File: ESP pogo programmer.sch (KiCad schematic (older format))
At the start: 3 parts

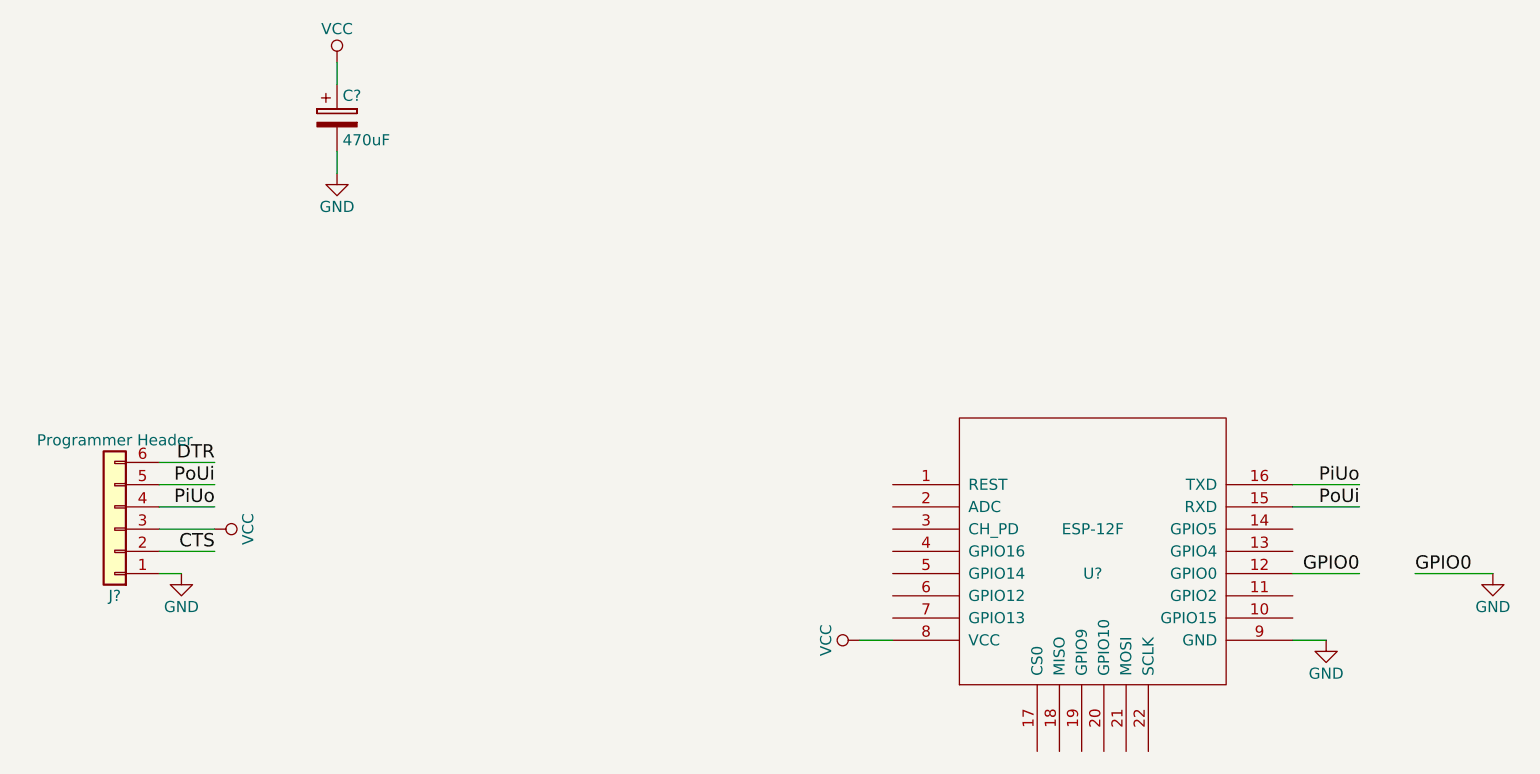
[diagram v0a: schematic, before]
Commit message: Schematic and footprints done
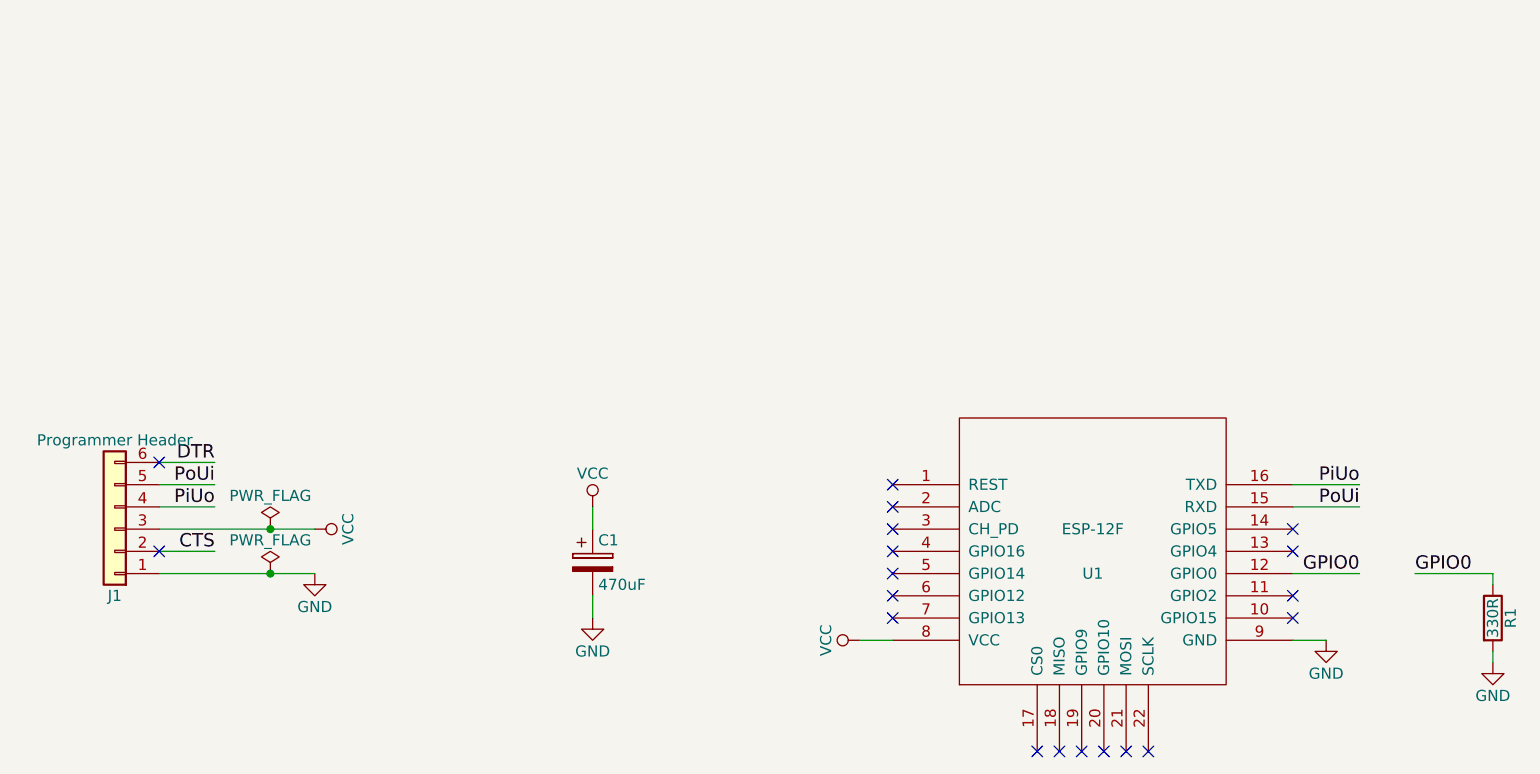
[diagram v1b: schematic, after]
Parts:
- added R1: 330R, Resistors_THT:R_Axial_DIN0207_L6.3mm_D2.5mm_P7.62mm_Horizontal, symbol R
- C1: renamed from C?; footprint (none) -> Capacitors_THT:CP_Radial_D6.3mm_P2.50mm
- J1: renamed from J?; footprint (none) -> Socket_Strips:Socket_Strip_Straight_1x06_Pitch2.54mm
- U1: renamed from U?; footprint (none) -> ESP-pogo-programmer_local:ESP-12F-pgrm
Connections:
- net GND: now also R1.2; no longer U1.12 (GPIO0)
- new net GPIO0: R1.1, U1.12 (GPIO0)
- no-connect marks 0 -> 19
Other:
- moved on the sheet: C1
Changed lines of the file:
@@
 $EndDescr
 $Comp
-L Conn_01x06 J?
+L Conn_01x06 J1
 U 1 1 5AC77FF5
 P 1550 3900
-F 0 "J?" H 1550 4200 50  0000 C CNN
+F 0 "J1" H 1550 4200 50  0000 C CNN
 F 1 "Programmer Header" H 1550 3500 50  0000 C CNN
-F 2 "" H 1550 3900 50  0001 C CNN
+F 2 "Socket_Strips:Socket_Strip_Straight_1x06_Pitch2.54mm" H 1550 3900 50  0001 C CNN
 F 3 "" H 1550 3900 50  0001 C CNN
 	1    1550 3900
@@
 $EndComp
 $Comp
-L GND #PWR?
+L GND #PWR01
 U 1 1 5AC78376
-P 1850 4100
-F 0 "#PWR?" H 1850 3850 50  0001 C CNN
-F 1 "GND" H 1850 3950 50  0000 C CNN
-F 2 "" H 1850 4100 50  0001 C CNN
-F 3 "" H 1850 4100 50  0001 C CNN
-	1    1850 4100
-	1    0    0    -1
-$EndComp
-Wire Wire Line
-	1750 4100 1850 4100
-$Comp
-L VCC #PWR?
+P 2450 4100
+F 0 "#PWR01" H 2450 3850 50  0001 C CNN
+F 1 "GND" H 2450 3950 50  0000 C CNN
+F 2 "" H 2450 4100 50  0001 C CNN
+F 3 "" H 2450 4100 50  0001 C CNN
+	1    2450 4100
+	1    0    0    -1
+$EndComp
+$Comp
+L VCC #PWR02
 U 1 1 5AC7838F
-P 2000 3900
-F 0 "#PWR?" H 2000 3750 50  0001 C CNN
-F 1 "VCC" H 2000 4050 50  0000 C CNN
-F 2 "" H 2000 3900 50  0001 C CNN
-F 3 "" H 2000 3900 50  0001 C CNN
-	1    2000 3900
+P 2450 3900
+F 0 "#PWR02" H 2450 3750 50  0001 C CNN
+F 1 "VCC" H 2450 4050 50  0000 C CNN
+F 2 "" H 2450 3900 50  0001 C CNN
+F 3 "" H 2450 3900 50  0001 C CNN
+	1    2450 3900
 	0    1    1    0
 $EndComp
-Wire Wire Line
-	1750 3900 2000 3900
 Text Label 2000 3800 2    60   ~ 0
 PiUo
@@
 	2000 3700 1750 3700
 $Comp
-L VCC #PWR?
+L VCC #PWR03
 U 1 1 5AC783EB
-P 2550 1800
-F 0 "#PWR?" H 2550 1650 50  0001 C CNN
-F 1 "VCC" H 2550 1950 50  0000 C CNN
-F 2 "" H 2550 1800 50  0001 C CNN
-F 3 "" H 2550 1800 50  0001 C CNN
-	1    2550 1800
-	1    0    0    -1
-$EndComp
-$Comp
-L CP C?
+P 3700 3800
+F 0 "#PWR03" H 3700 3650 50  0001 C CNN
+F 1 "VCC" H 3700 3950 50  0000 C CNN
+F 2 "" H 3700 3800 50  0001 C CNN
+F 3 "" H 3700 3800 50  0001 C CNN
+	1    3700 3800
+	1    0    0    -1
+$EndComp
+$Comp
+L CP C1
 U 1 1 5AC78401
-P 2550 2050
-F 0 "C?" H 2575 2150 50  0000 L CNN
-F 1 "470uF" H 2575 1950 50  0000 L CNN
-F 2 "" H 2588 1900 50  0001 C CNN
-F 3 "" H 2550 2050 50  0001 C CNN
-	1    2550 2050
-	1    0    0    -1
-$EndComp
-$Comp
-L GND #PWR?
+P 3700 4050
+F 0 "C1" H 3725 4150 50  0000 L CNN
+F 1 "470uF" H 3725 3950 50  0000 L CNN
+F 2 "Capacitors_THT:CP_Radial_D6.3mm_P2.50mm" H 3738 3900 50  0001 C CNN
+F 3 "" H 3700 4050 50  0001 C CNN
+	1    3700 4050
+	1    0    0    -1
+$EndComp
+$Comp
+L GND #PWR04
 U 1 1 5AC78426
-P 2550 2300
-F 0 "#PWR?" H 2550 2050 50  0001 C CNN
-F 1 "GND" H 2550 2150 50  0000 C CNN
-F 2 "" H 2550 2300 50  0001 C CNN
-F 3 "" H 2550 2300 50  0001 C CNN
-	1    2550 2300
-	1    0    0    -1
-$EndComp
-Wire Wire Line
-	2550 2300 2550 2200
-Wire Wire Line
-	2550 1900 2550 1800
-$Comp
-L ESP-12F U?
+P 3700 4300
+F 0 "#PWR04" H 3700 4050 50  0001 C CNN
+F 1 "GND" H 3700 4150 50  0000 C CNN
+F 2 "" H 3700 4300 50  0001 C CNN
+F 3 "" H 3700 4300 50  0001 C CNN
+	1    3700 4300
+	1    0    0    -1
+$EndComp
+Wire Wire Line
+	3700 4300 3700 4200
+Wire Wire Line
+	3700 3900 3700 3800
+$Comp
+L ESP-12F U1
 U 1 1 5AC785DC
 P 5950 4000
-F 0 "U?" H 5950 3900 50  0000 C CNN
+F 0 "U1" H 5950 3900 50  0000 C CNN
 F 1 "ESP-12F" H 5950 4100 50  0000 C CNN
-F 2 "" H 5950 4000 50  0001 C CNN
+F 2 "ESP-pogo-programmer_local:ESP-12F-pgrm" H 5950 4000 50  0001 C CNN
 F 3 "" H 5950 4000 50  0001 C CNN
 	1    5950 4000
@@
 	7150 3700 6850 3700
 $Comp
-L GND #PWR?
+L GND #PWR05
 U 1 1 5AC78725
 P 7000 4400
-F 0 "#PWR?" H 7000 4150 50  0001 C CNN
+F 0 "#PWR05" H 7000 4150 50  0001 C CNN
 F 1 "GND" H 7000 4250 50  0000 C CNN
 F 2 "" H 7000 4400 50  0001 C CNN
@@
 	6850 4400 7000 4400
 $Comp
-L VCC #PWR?
+L VCC #PWR06
 U 1 1 5AC7874E
 P 4900 4400
-F 0 "#PWR?" H 4900 4250 50  0001 C CNN
+F 0 "#PWR06" H 4900 4250 50  0001 C CNN
 F 1 "VCC" H 4900 4550 50  0000 C CNN
 F 2 "" H 4900 4400 50  0001 C CNN
@@
 GPIO0
 $Comp
-L GND #PWR?
+L GND #PWR07
 U 1 1 5AC7A389
-P 7750 4100
-F 0 "#PWR?" H 7750 3850 50  0001 C CNN
-F 1 "GND" H 7750 3950 50  0000 C CNN
-F 2 "" H 7750 4100 50  0001 C CNN
-F 3 "" H 7750 4100 50  0001 C CNN
-	1    7750 4100
+P 7750 4500
+F 0 "#PWR07" H 7750 4250 50  0001 C CNN
+F 1 "GND" H 7750 4350 50  0000 C CNN
+F 2 "" H 7750 4500 50  0001 C CNN
+F 3 "" H 7750 4500 50  0001 C CNN
+	1    7750 4500
 	1    0    0    -1
 $EndComp
 Wire Wire Line
 	7750 4100 7400 4100
+$Comp
+L R R1
+U 1 1 5AD0EC53
+P 7750 4300
+F 0 "R1" V 7830 4300 50  0000 C CNN
+F 1 "330R" V 7750 4300 50  0000 C CNN
+F 2 "Resistors_THT:R_Axial_DIN0207_L6.3mm_D2.5mm_P7.62mm_Horizontal" V 7680 4300 50  0001 C CNN
+F 3 "" H 7750 4300 50  0001 C CNN
+	1    7750 4300
+	1    0    0    -1
+$EndComp
+Wire Wire Line
+	7750 4100 7750 4150
+Wire Wire Line
+	7750 4450 7750 4500
+NoConn ~ 1750 4000
+NoConn ~ 1750 3600
+NoConn ~ 5050 3700
+NoConn ~ 5050 3800
+NoConn ~ 5050 3900
+NoConn ~ 5050 4000
+NoConn ~ 5050 4100
+NoConn ~ 5050 4200
+NoConn ~ 5050 4300
+NoConn ~ 5700 4900
+NoConn ~ 5800 4900
+NoConn ~ 5900 4900
+NoConn ~ 6000 4900
+NoConn ~ 6100 4900
+NoConn ~ 6200 4900
+NoConn ~ 6850 4300
+NoConn ~ 6850 4200
+NoConn ~ 6850 3900
+NoConn ~ 6850 4000
+$Comp
+L PWR_FLAG #FLG08
+U 1 1 5AD104B9
+P 2250 3900
+F 0 "#FLG08" H 2250 3975 50  0001 C CNN
+F 1 "PWR_FLAG" H 2250 4050 50  0000 C CNN
+F 2 "" H 2250 3900 50  0001 C CNN
+F 3 "" H 2250 3900 50  0001 C CNN
+	1    2250 3900
+	1    0    0    -1
+$EndComp
+Wire Wire Line
+	1750 3900 2450 3900
+Connection ~ 2250 3900
+$Comp
+L PWR_FLAG #FLG09
+U 1 1 5AD105BA
+P 2250 4100
+F 0 "#FLG09" H 2250 4175 50  0001 C CNN
+F 1 "PWR_FLAG" H 2250 4250 50  0000 C CNN
+F 2 "" H 2250 4100 50  0001 C CNN
+F 3 "" H 2250 4100 50  0001 C CNN
+	1    2250 4100
+	1    0    0    -1
+$EndComp
+Wire Wire Line
+	1750 4100 2450 4100
+Connection ~ 2250 4100
 $EndSCHEMATC
